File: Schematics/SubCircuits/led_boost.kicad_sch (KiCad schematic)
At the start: 7 parts, among them J5 ADDR_LED, J6 LED

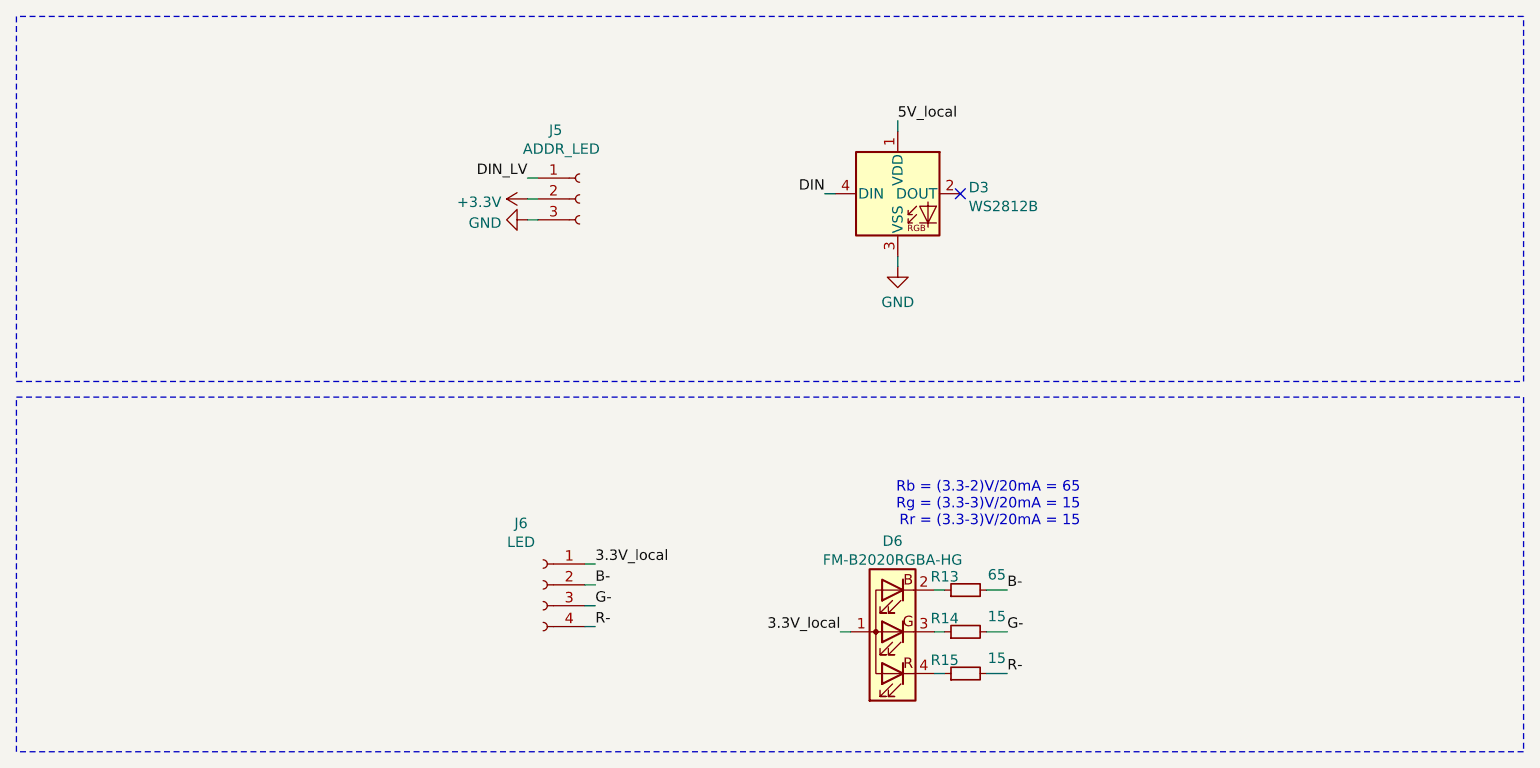
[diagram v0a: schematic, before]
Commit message: Added defunct subcircuit project
superseded by modular mainboard
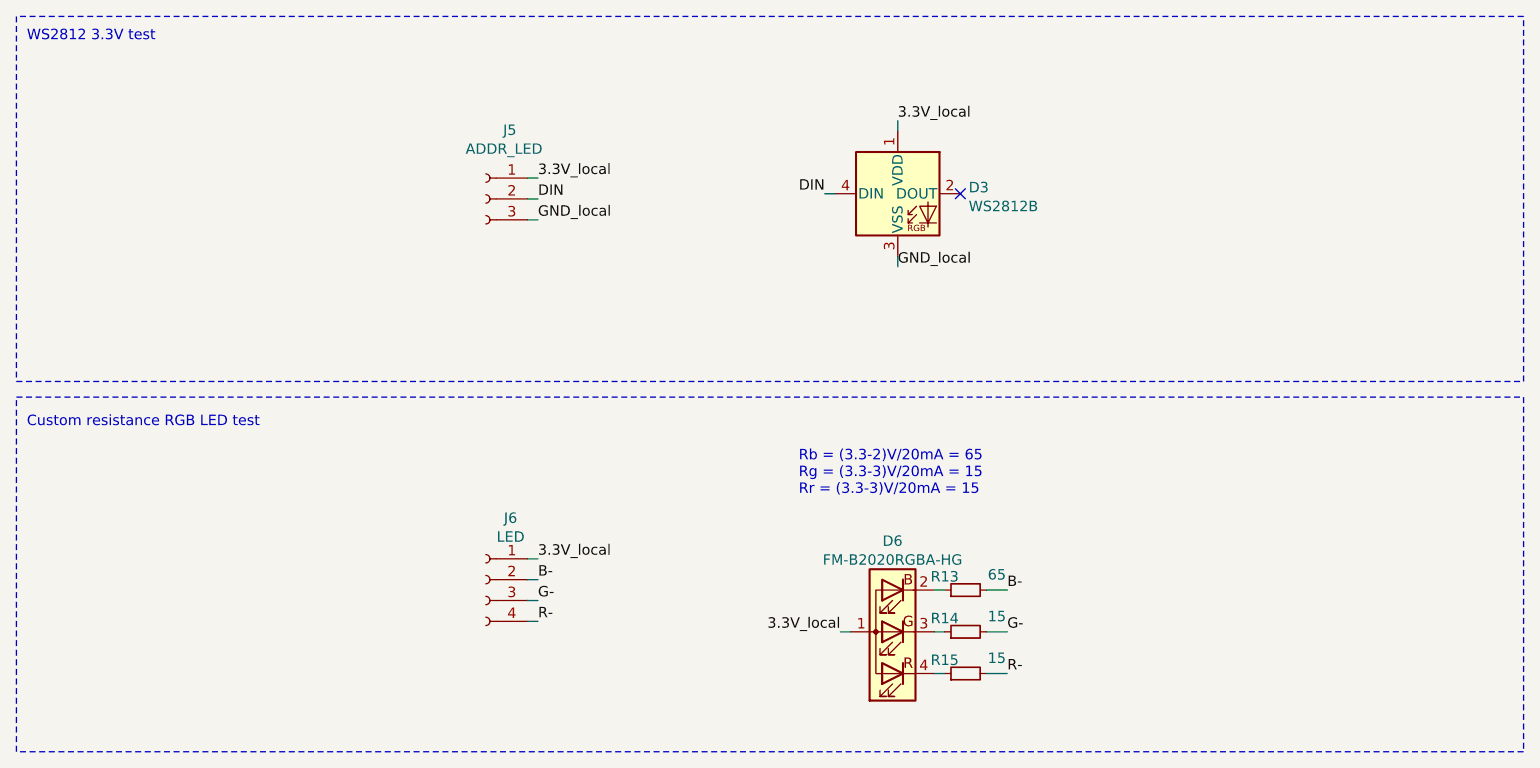
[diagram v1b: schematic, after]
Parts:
- D3: LCSC Part C965555 -> C965555
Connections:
- net +3V3 is gone; now on net DIN: J5.2 (Pin_2)
- net 5V_local is gone; now on net 3.3V_local: D3.1 (VDD)
- net DIN_LV is gone; now on net 3.3V_local: J5.1 (Pin_1)
- net GND renamed GND_local
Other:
- note added: "Custom resistance RGB LED test"
- note added: "WS2812 3.3V test"
- moved on the sheet: J5, J6
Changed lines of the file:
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@@
-(kicad_sch (version 20210126) (generator eeschema)
+(kicad_sch (version 20210406) (generator eeschema)
   (paper "A5")
   (no_connect (at 128.27 34.925))
-  (wire (pts (xy 75.565 33.02) (xy 76.835 33.02))
-    (stroke (width 0) (type solid) (color 0 0 0 0))
-  )
-  (wire (pts (xy 75.565 35.56) (xy 76.835 35.56))
-    (stroke (width 0) (type solid) (color 0 0 0 0))
-  )
-  (wire (pts (xy 75.565 38.1) (xy 76.835 38.1))
-    (stroke (width 0) (type solid) (color 0 0 0 0))
-  )
-  (wire (pts (xy 82.55 80.01) (xy 83.82 80.01))
-    (stroke (width 0) (type solid) (color 0 0 0 0))
-  )
-  (wire (pts (xy 82.55 82.55) (xy 83.82 82.55))
-    (stroke (width 0) (type solid) (color 0 0 0 0))
-  )
-  (wire (pts (xy 82.55 85.09) (xy 83.82 85.09))
-    (stroke (width 0) (type solid) (color 0 0 0 0))
-  )
-  (wire (pts (xy 82.55 87.63) (xy 83.82 87.63))
+  (wire (pts (xy 75.565 79.375) (xy 76.835 79.375))
+    (stroke (width 0) (type solid) (color 0 0 0 0))
+  )
+  (wire (pts (xy 75.565 81.915) (xy 76.835 81.915))
+    (stroke (width 0) (type solid) (color 0 0 0 0))
+  )
+  (wire (pts (xy 75.565 84.455) (xy 76.835 84.455))
+    (stroke (width 0) (type solid) (color 0 0 0 0))
+  )
+  (wire (pts (xy 75.565 86.995) (xy 76.835 86.995))
+    (stroke (width 0) (type solid) (color 0 0 0 0))
+  )
+  (wire (pts (xy 76.835 33.02) (xy 75.565 33.02))
+    (stroke (width 0) (type solid) (color 0 0 0 0))
+  )
+  (wire (pts (xy 76.835 35.56) (xy 75.565 35.56))
+    (stroke (width 0) (type solid) (color 0 0 0 0))
+  )
+  (wire (pts (xy 76.835 38.1) (xy 75.565 38.1))
     (stroke (width 0) (type solid) (color 0 0 0 0))
   )
@@
     (stroke (width 0) (type dash) (color 0 0 0 0))
   )
+  (text "WS2812 3.3V test" (at 14.605 16.51 0)
+    (effects (font (size 1.27 1.27)) (justify left bottom))
+  )
+  (text "Custom resistance RGB LED test" (at 14.605 63.5 0)
+    (effects (font (size 1.27 1.27)) (justify left bottom))
+  )
   (text "Rb = (3.3-2)V/20mA = 65\nRg = (3.3-3)V/20mA = 15\nRr = (3.3-3)V/20mA = 15"
-    (at 142.875 75.565 0)
-    (effects (font (size 1.27 1.27)) (justify right bottom))
-  )
-  (label "DIN_LV" (at 75.565 33.02 180)
-    (effects (font (size 1.27 1.27)) (justify right bottom))
-  )
-  (label "3.3V_local" (at 83.82 80.01 0)
-    (effects (font (size 1.27 1.27)) (justify left bottom))
-  )
-  (label "B-" (at 83.82 82.55 0)
-    (effects (font (size 1.27 1.27)) (justify left bottom))
-  )
-  (label "G-" (at 83.82 85.09 0)
-    (effects (font (size 1.27 1.27)) (justify left bottom))
-  )
-  (label "R-" (at 83.82 87.63 0)
+    (at 108.585 71.755 0)
+    (effects (font (size 1.27 1.27)) (justify left bottom))
+  )
+  (label "3.3V_local" (at 76.835 33.02 0)
+    (effects (font (size 1.27 1.27)) (justify left bottom))
+  )
+  (label "DIN" (at 76.835 35.56 0)
+    (effects (font (size 1.27 1.27)) (justify left bottom))
+  )
+  (label "GND_local" (at 76.835 38.1 0)
+    (effects (font (size 1.27 1.27)) (justify left bottom))
+  )
+  (label "3.3V_local" (at 76.835 79.375 0)
+    (effects (font (size 1.27 1.27)) (justify left bottom))
+  )
+  (label "B-" (at 76.835 81.915 0)
+    (effects (font (size 1.27 1.27)) (justify left bottom))
+  )
+  (label "G-" (at 76.835 84.455 0)
+    (effects (font (size 1.27 1.27)) (justify left bottom))
+  )
+  (label "R-" (at 76.835 86.995 0)
     (effects (font (size 1.27 1.27)) (justify left bottom))
   )
@@
     (effects (font (size 1.27 1.27)) (justify right bottom))
   )
-  (label "5V_local" (at 120.65 26.035 0)
+  (label "3.3V_local" (at 120.65 26.035 0)
+    (effects (font (size 1.27 1.27)) (justify left bottom))
+  )
+  (label "GND_local" (at 120.65 43.815 0)
     (effects (font (size 1.27 1.27)) (justify left bottom))
   )
@@
   (label "R-" (at 133.985 93.345 0)
     (effects (font (size 1.27 1.27)) (justify left bottom))
-  )
-  (symbol (lib_id "power:+3.3V") (at 75.565 35.56 90) (mirror x) (unit 1)
-    (in_bom yes) (on_board yes)
-    (property "Reference" "#PWR0124" (id 0) (at 79.375 35.56 0)
-      (effects (font (size 1.27 1.27)) hide)
-    )
-    (property "Value" "+3.3V" (id 1) (at 72.3899 35.9485 90)
-      (effects (font (size 1.27 1.27)) (justify left))
-    )
-    (property "Footprint" "" (id 2) (at 75.565 35.56 0)
-      (effects (font (size 1.27 1.27)) hide)
-    )
-    (property "Datasheet" "" (id 3) (at 75.565 35.56 0)
-      (effects (font (size 1.27 1.27)) hide)
-    )
-    (pin "1")
-  )
-  (symbol (lib_id "power:GND") (at 75.565 38.1 270) (unit 1)
-    (in_bom yes) (on_board yes)
-    (property "Reference" "#PWR0135" (id 0) (at 69.215 38.1 0)
-      (effects (font (size 1.27 1.27)) hide)
-    )
-    (property "Value" "GND" (id 1) (at 72.39 38.4885 90)
-      (effects (font (size 1.27 1.27)) (justify right))
-    )
-    (property "Footprint" "" (id 2) (at 75.565 38.1 0)
-      (effects (font (size 1.27 1.27)) hide)
-    )
-    (property "Datasheet" "" (id 3) (at 75.565 38.1 0)
-      (effects (font (size 1.27 1.27)) hide)
-    )
-    (pin "1")
-  )
-  (symbol (lib_id "power:GND") (at 120.65 43.815 0) (unit 1)
-    (in_bom yes) (on_board yes)
-    (property "Reference" "#PWR0126" (id 0) (at 120.65 50.165 0)
-      (effects (font (size 1.27 1.27)) hide)
-    )
-    (property "Value" "GND" (id 1) (at 120.65 48.1394 0))
-    (property "Footprint" "" (id 2) (at 120.65 43.815 0)
-      (effects (font (size 1.27 1.27)) hide)
-    )
-    (property "Datasheet" "" (id 3) (at 120.65 43.815 0)
-      (effects (font (size 1.27 1.27)) hide)
-    )
-    (pin "1")
   )
   (symbol (lib_id "Device:R_Small") (at 128.905 83.185 90) (unit 1)
@@
     (pin "2")
   )
-  (symbol (lib_id "Connector:Conn_01x03_Female") (at 81.915 35.56 0) (unit 1)
-    (in_bom yes) (on_board yes)
-    (property "Reference" "J5" (id 0) (at 78.1813 27.1791 0)
-      (effects (font (size 1.27 1.27)) (justify left))
-    )
-    (property "Value" "ADDR_LED" (id 1) (at 75.0063 29.4778 0)
-      (effects (font (size 1.27 1.27)) (justify left))
-    )
-    (property "Footprint" "Connector_PinSocket_2.54mm:PinSocket_1x03_P2.54mm_Vertical" (id 2) (at 81.915 35.56 0)
-      (effects (font (size 1.27 1.27)) hide)
-    )
-    (property "Datasheet" "~" (id 3) (at 81.915 35.56 0)
+  (symbol (lib_id "Connector:Conn_01x03_Female") (at 70.485 35.56 0) (mirror y) (unit 1)
+    (in_bom yes) (on_board yes)
+    (property "Reference" "J5" (id 0) (at 74.2187 27.1791 0)
+      (effects (font (size 1.27 1.27)) (justify left))
+    )
+    (property "Value" "ADDR_LED" (id 1) (at 77.3937 29.4778 0)
+      (effects (font (size 1.27 1.27)) (justify left))
+    )
+    (property "Footprint" "Connector_PinSocket_2.54mm:PinSocket_1x03_P2.54mm_Vertical" (id 2) (at 70.485 35.56 0)
+      (effects (font (size 1.27 1.27)) hide)
+    )
+    (property "Datasheet" "~" (id 3) (at 70.485 35.56 0)
       (effects (font (size 1.27 1.27)) hide)
     )
@@
     (pin "3")
   )
-  (symbol (lib_id "Connector:Conn_01x04_Female") (at 77.47 82.55 0) (mirror y) (unit 1)
-    (in_bom yes) (on_board yes)
-    (property "Reference" "J6" (id 0) (at 74.7776 75.0528 0))
-    (property "Value" "LED" (id 1) (at 74.7776 77.3515 0))
-    (property "Footprint" "Connector_PinHeader_2.54mm:PinHeader_1x04_P2.54mm_Vertical" (id 2) (at 77.47 82.55 0)
-      (effects (font (size 1.27 1.27)) hide)
-    )
-    (property "Datasheet" "~" (id 3) (at 77.47 82.55 0)
+  (symbol (lib_id "Connector:Conn_01x04_Female") (at 70.485 81.915 0) (mirror y) (unit 1)
+    (in_bom yes) (on_board yes)
+    (property "Reference" "J6" (id 0) (at 73.5076 74.4178 0))
+    (property "Value" "LED" (id 1) (at 73.5076 76.7165 0))
+    (property "Footprint" "Connector_PinHeader_2.54mm:PinHeader_1x04_P2.54mm_Vertical" (id 2) (at 70.485 81.915 0)
+      (effects (font (size 1.27 1.27)) hide)
+    )
+    (property "Datasheet" "~" (id 3) (at 70.485 81.915 0)
       (effects (font (size 1.27 1.27)) hide)
     )
@@
       (effects (font (size 1.27 1.27)) (justify left top) hide)
     )
-    (property "LCSC Part" " C965555" (id 4) (at 120.65 34.925 0)
-      (effects (font (size 1.27 1.27)) hide)
-    )
+    (property "LCSC Part" "C965555" (id 4) (at 120.65 34.925 0)
+      (effects (font (size 1.27 1.27)) hide)
+    )
